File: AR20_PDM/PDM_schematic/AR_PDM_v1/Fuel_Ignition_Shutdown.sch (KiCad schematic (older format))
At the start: 16 parts

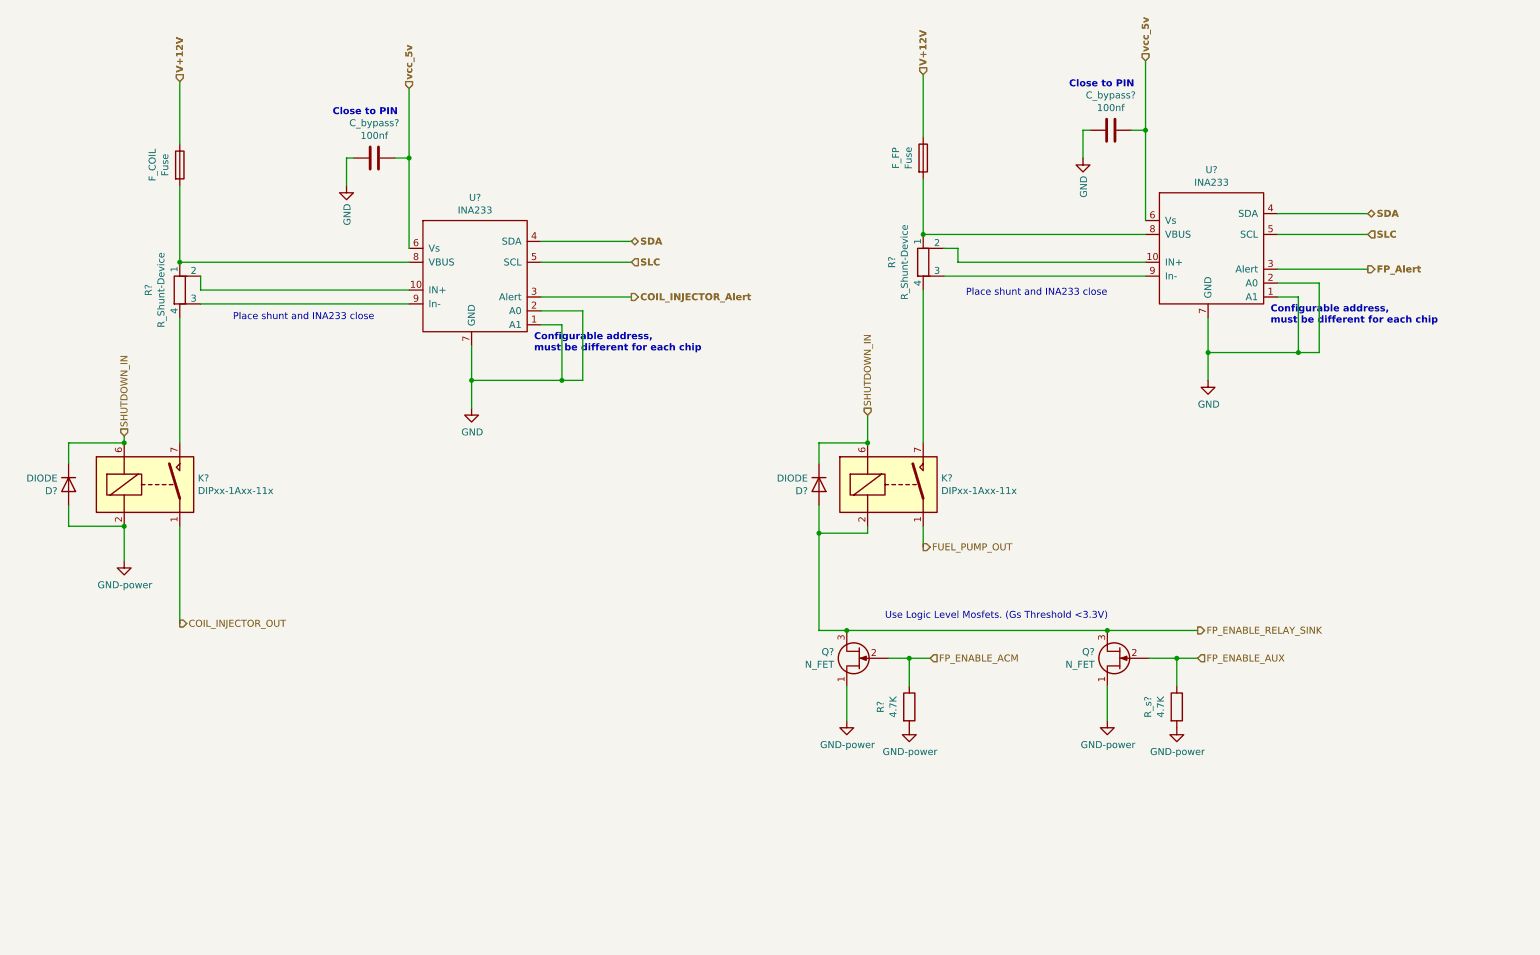
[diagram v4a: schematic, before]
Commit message: Fixed issues, controlled components, BOM, see discription
- added acm symbol
- fixed wrongly faced P-mosfets
- I/O expander now sinks led instead of source
- Bill of material mostly done
- Correct address for INA233 chips.
- Now 4 diodes serves as flyback for all mosfets
- Corrected naming scheme for compmonents (everything is not fixed yet)
- Fixed some labels
- altso some minor changes
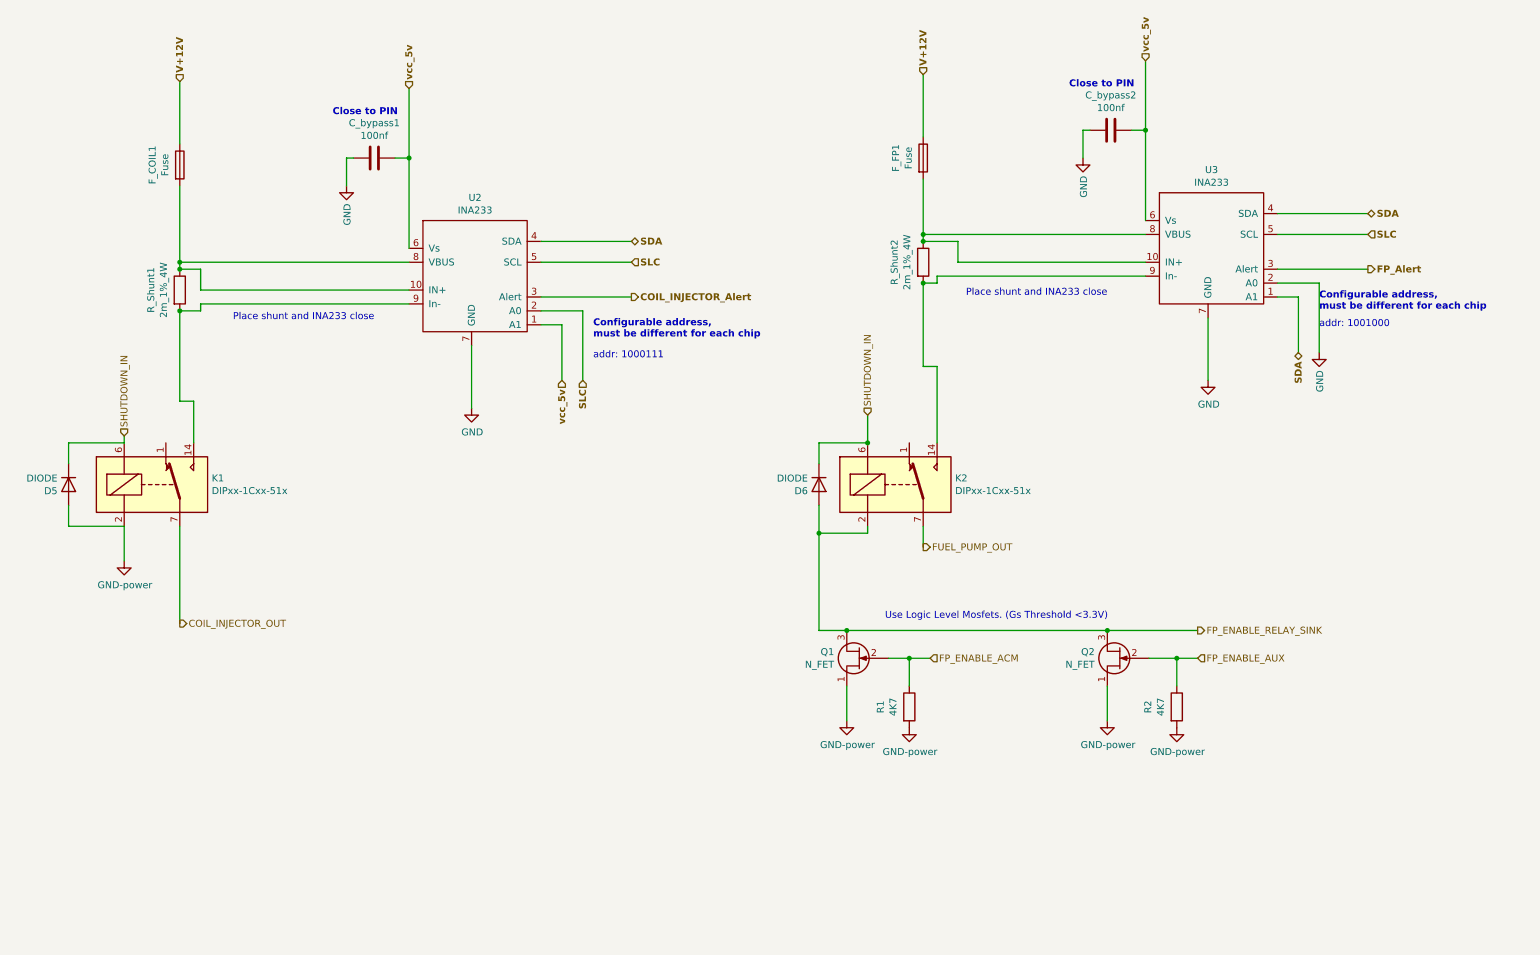
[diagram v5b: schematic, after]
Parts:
- removed K? (x2): DIPxx-1Axx-11x, Relay_THT:Relay_StandexMeder_DIP_LowProfile, symbol Relay:DIPxx-1Axx-11x
- removed R? (x2): R_Shunt-Device, symbol AR20_PDM_v1-rescue:R_Shunt-Device
- added K1, K2: DIPxx-1Cxx-51x, Relay_THT:Relay_StandexMeder_DIP_LowProfile, symbol Relay:DIPxx-1Cxx-51x
- added R_Shunt1, R_Shunt2: 2m_1%_4W, symbol AR20_PDM_v1-rescue:R-Device
- C_bypass1, C_bypass2: renamed from C_bypass?; footprint (none) -> Capacitor_SMD:C_0603_1608Metric
- R1, R2: renamed from R?; value 4.7K -> 4K7
- gave numbers to parts that had none: 6
- renumbered F_COIL to F_COIL1, F_FP to F_FP1
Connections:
- net COIL_INJECTOR_OUT: now also K1.7, K1.8
- net FP_ENABLE_RELAY_SINK: now also K2.2
- net FUEL_PUMP_OUT: now also K2.7, K2.8
- net GND: now also K1.2; no longer U2.1 (A1), U2.2 (A0), U3.1 (A1)
- net SDA: now also U3.1 (A1)
- net SHUTDOWN_IN: now also K1.6, K2.6
- net SLC: now also U2.2 (A0)
- net vcc_5v: now also U2.1 (A1)
- net at F_COIL1.2, U2.8 (VBUS): now also U2.10 (IN+), R_Shunt1.1
- net at U2.9 (In-): now also K1.14, R_Shunt1.2
- net at F_FP1.2, U3.8 (VBUS): now also U3.10 (IN+), R_Shunt2.1
- net at U3.9 (In-): now also K2.14, R_Shunt2.2
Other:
- note added: "addr: 1000111"
- note added: "addr: 1001000"

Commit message: PCB design, and issue fixing, work in progress
- Error fixed: Mux mosfet resistor change to ground
- Open drain output added on phase 6, for engine blipping purpose
- Most of pcb symbols and footprints are finished, including main connector
- PCB is change from 1oz to 2oz copper layer, for easier routing.
- Basic Draft of pcb is done, for now.
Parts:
- D5, D6: footprint (none) -> AR_PDM_v1:SODFL2512X73N; symbol AR20_PDM_v1-rescue:DIODE-Simulation_SPICE -> AR20_PDM_v1-rescue:DIODE-CustomSymbol
- F_COIL1, F_FP1: footprint (none) -> AR_PDM_v1:FuseHolder
- K1, K2: footprint Relay_THT:Relay_StandexMeder_DIP_LowProfile -> AR_PDM_v1:Relay; symbol Relay:DIPxx-1Cxx-51x -> AR20_PDM_v1-rescue:Relay
- Q8: renamed from Q1; footprint (none) -> Package_TO_SOT_SMD:SOT-23
- Q9: renamed from Q2; footprint (none) -> Package_TO_SOT_SMD:SOT-23
- R1, R2: footprint (none) -> Resistor_SMD:R_0603_1608Metric
- R_Shunt1, R_Shunt2: footprint (none) -> Resistor_SMD:R_2512_6332Metric
- U2, U3: footprint (none) -> AR_PDM_v1:INA233
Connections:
- net COIL_INJECTOR_OUT: no longer K1.8
- net FP_ENABLE_RELAY_SINK: now also D6.2 (A); no longer D6.1 (A)
- net FUEL_PUMP_OUT: no longer K2.8
- net GND: now also D5.2 (A); no longer D5.1 (A)
- net SHUTDOWN_IN: now also D5.1 (K), D6.1 (K); no longer D5.2 (K), D6.2 (K)
- no-connect marks 0 -> 2
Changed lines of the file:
@@
 	7350 4250 7350 4400
 $Comp
-L Device:Q_NJFET_DGS Q1
+L Device:Q_NJFET_DGS Q8
 U 1 1 5DDCBB71
 P 6900 5200
-F 0 "Q1" H 7091 5154 50  0000 L CNN
+F 0 "Q8" H 7091 5154 50  0000 L CNN
 F 1 "N_FET" H 7091 5245 50  0000 L CNN
-F 2 "" H 7100 5300 50  0001 C CNN
+F 2 "Package_TO_SOT_SMD:SOT-23" H 7100 5300 50  0001 C CNN
 F 3 "~" H 6900 5200 50  0001 C CNN
 	1    6900 5200
@@
 SHUTDOWN_IN
 $Comp
-L AR20_PDM_v1-rescue:DIODE-Simulation_SPICE D6
+L AR20_PDM_v1-rescue:DIODE-CustomSymbol D6
 U 1 1 5DDDEC0F
 P 6600 3950
 F 0 "D6" V 6554 4030 50  0000 L CNN
 F 1 "DIODE" V 6645 4030 50  0000 L CNN
-F 2 "" H 6600 3950 50  0001 C CNN
+F 2 "AR_PDM_v1:SODFL2512X73N" H 6600 3950 50  0001 C CNN
 F 3 "" H 6600 3950 50  0001 C CNN
 F 4 "Y" H 6600 3950 50  0001 L CNN "Spice_Netlist_Enabled"
@@
 	6800 5400 6800 5650
 $Comp
-L Device:Q_NJFET_DGS Q2
+L Device:Q_NJFET_DGS Q9
 U 1 1 5DDB5A55
 P 8775 5200
-F 0 "Q2" H 8966 5154 50  0000 L CNN
+F 0 "Q9" H 8966 5154 50  0000 L CNN
 F 1 "N_FET" H 8966 5245 50  0000 L CNN
-F 2 "" H 8975 5300 50  0001 C CNN
+F 2 "Package_TO_SOT_SMD:SOT-23" H 8975 5300 50  0001 C CNN
 F 3 "~" H 8775 5200 50  0001 C CNN
 	1    8775 5200
@@
 F 0 "R2" V 8968 5550 50  0000 C CNN
 F 1 "4K7" V 9059 5550 50  0000 C CNN
-F 2 "" V 9105 5550 50  0001 C CNN
+F 2 "Resistor_SMD:R_0603_1608Metric" V 9105 5550 50  0001 C CNN
 F 3 "~" H 9175 5550 50  0001 C CNN
 	1    9175 5550
@@
 F 0 "R1" V 7043 5550 50  0000 C CNN
 F 1 "4K7" V 7134 5550 50  0000 C CNN
-F 2 "" V 7180 5550 50  0001 C CNN
+F 2 "Resistor_SMD:R_0603_1608Metric" V 7180 5550 50  0001 C CNN
 F 3 "~" H 7250 5550 50  0001 C CNN
 	1    7250 5550
@@
 F 0 "F_FP1" V 7153 1600 50  0000 C CNN
 F 1 "Fuse" V 7244 1600 50  0000 C CNN
-F 2 "" V 7280 1600 50  0001 C CNN
+F 2 "AR_PDM_v1:FuseHolder" V 7280 1600 50  0001 C CNN
 F 3 "~" H 7350 1600 50  0001 C CNN
 	1    7350 1600
@@
 F 0 "U3" H 9425 2515 50  0000 C CNN
 F 1 "INA233" H 9425 2424 50  0000 C CNN
-F 2 "" H 9400 2100 50  0001 C CNN
+F 2 "AR_PDM_v1:INA233" H 9400 2100 50  0001 C CNN
 F 3 "" H 9400 2100 50  0001 C CNN
 	1    9400 2100
@@
 F 0 "U2" H 4125 2715 50  0000 C CNN
 F 1 "INA233" H 4125 2624 50  0000 C CNN
-F 2 "" H 4100 2300 50  0001 C CNN
+F 2 "AR_PDM_v1:INA233" H 4100 2300 50  0001 C CNN
 F 3 "" H 4100 2300 50  0001 C CNN
 	1    4100 2300
@@
 	1200 3650 1200 3800
 $Comp
-L AR20_PDM_v1-rescue:DIODE-Simulation_SPICE D5
+L AR20_PDM_v1-rescue:DIODE-CustomSymbol D5
 U 1 1 5DDCE100
 P 1200 3950
 F 0 "D5" V 1154 4030 50  0000 L CNN
 F 1 "DIODE" V 1245 4030 50  0000 L CNN
-F 2 "" H 1200 3950 50  0001 C CNN
+F 2 "AR_PDM_v1:SODFL2512X73N" H 1200 3950 50  0001 C CNN
 F 3 "" H 1200 3950 50  0001 C CNN
 F 4 "Y" H 1200 3950 50  0001 L CNN "Spice_Netlist_Enabled"
@@
 F 0 "F_COIL1" V 1803 1650 50  0000 C CNN
 F 1 "Fuse" V 1894 1650 50  0000 C CNN
-F 2 "" V 1930 1650 50  0001 C CNN
+F 2 "AR_PDM_v1:FuseHolder" V 1930 1650 50  0001 C CNN
 F 3 "~" H 2000 1650 50  0001 C CNN
 	1    2000 1650
@@
 F 0 "R_Shunt1" V 1793 2550 50  0000 C CNN
 F 1 "2m_1%_4W" V 1884 2550 50  0000 C CNN
-F 2 "" V 1930 2550 50  0001 C CNN
+F 2 "Resistor_SMD:R_2512_6332Metric" V 1930 2550 50  0001 C CNN
 F 3 "~" H 2000 2550 50  0001 C CNN
 	1    2000 2550
@@
 F 0 "R_Shunt2" V 7143 2350 50  0000 C CNN
 F 1 "2m_1%_4W" V 7234 2350 50  0000 C CNN
-F 2 "" V 7280 2350 50  0001 C CNN
+F 2 "Resistor_SMD:R_2512_6332Metric" V 7280 2350 50  0001 C CNN
 F 3 "~" H 7350 2350 50  0001 C CNN
 	1    7350 2350
@@
 	7350 2200 7600 2200
 $Comp
-L Relay:DIPxx-1Cxx-51x K2
+L AR20_PDM_v1-rescue:Relay K?
 U 1 1 5E1CE6DB
 P 7150 3950
+AR Path="/5E1CE6DB" Ref="K?"  Part="1"
+AR Path="/5DA8920B/5E1CE6DB" Ref="K2"  Part="1"
 F 0 "K2" H 7580 3996 50  0000 L CNN
 F 1 "DIPxx-1Cxx-51x" H 7580 3905 50  0000 L CNN
-F 2 "Relay_THT:Relay_StandexMeder_DIP_LowProfile" H 7600 3900 50  0001 L CNN
+F 2 "AR_PDM_v1:Relay" H 7600 3900 50  0001 L CNN
 F 3 "https://standexelectronics.com/wp-content/uploads/datasheet_reed_relay_DIP.pdf" H 7150 3950 50  0001 C CNN
 	1    7150 3950
@@
 Connection ~ 7350 2500
 $Comp
-L Relay:DIPxx-1Cxx-51x K1
+L AR20_PDM_v1-rescue:Relay K?
 U 1 1 5E1D8A96
 P 1800 3950
+AR Path="/5E1D8A96" Ref="K?"  Part="1"
+AR Path="/5DA8920B/5E1D8A96" Ref="K1"  Part="1"
 F 0 "K1" H 2230 3996 50  0000 L CNN
 F 1 "DIPxx-1Cxx-51x" H 2230 3905 50  0000 L CNN
-F 2 "Relay_THT:Relay_StandexMeder_DIP_LowProfile" H 2250 3900 50  0001 L CNN
+F 2 "AR_PDM_v1:Relay" H 2250 3900 50  0001 L CNN
 F 3 "https://standexelectronics.com/wp-content/uploads/datasheet_reed_relay_DIP.pdf" H 1800 3950 50  0001 C CNN
 	1    1800 3950
@@
 	1    0    0    -1
 $EndComp
+NoConn ~ 7250 3650
+NoConn ~ 1900 3650
 $EndSCHEMATC

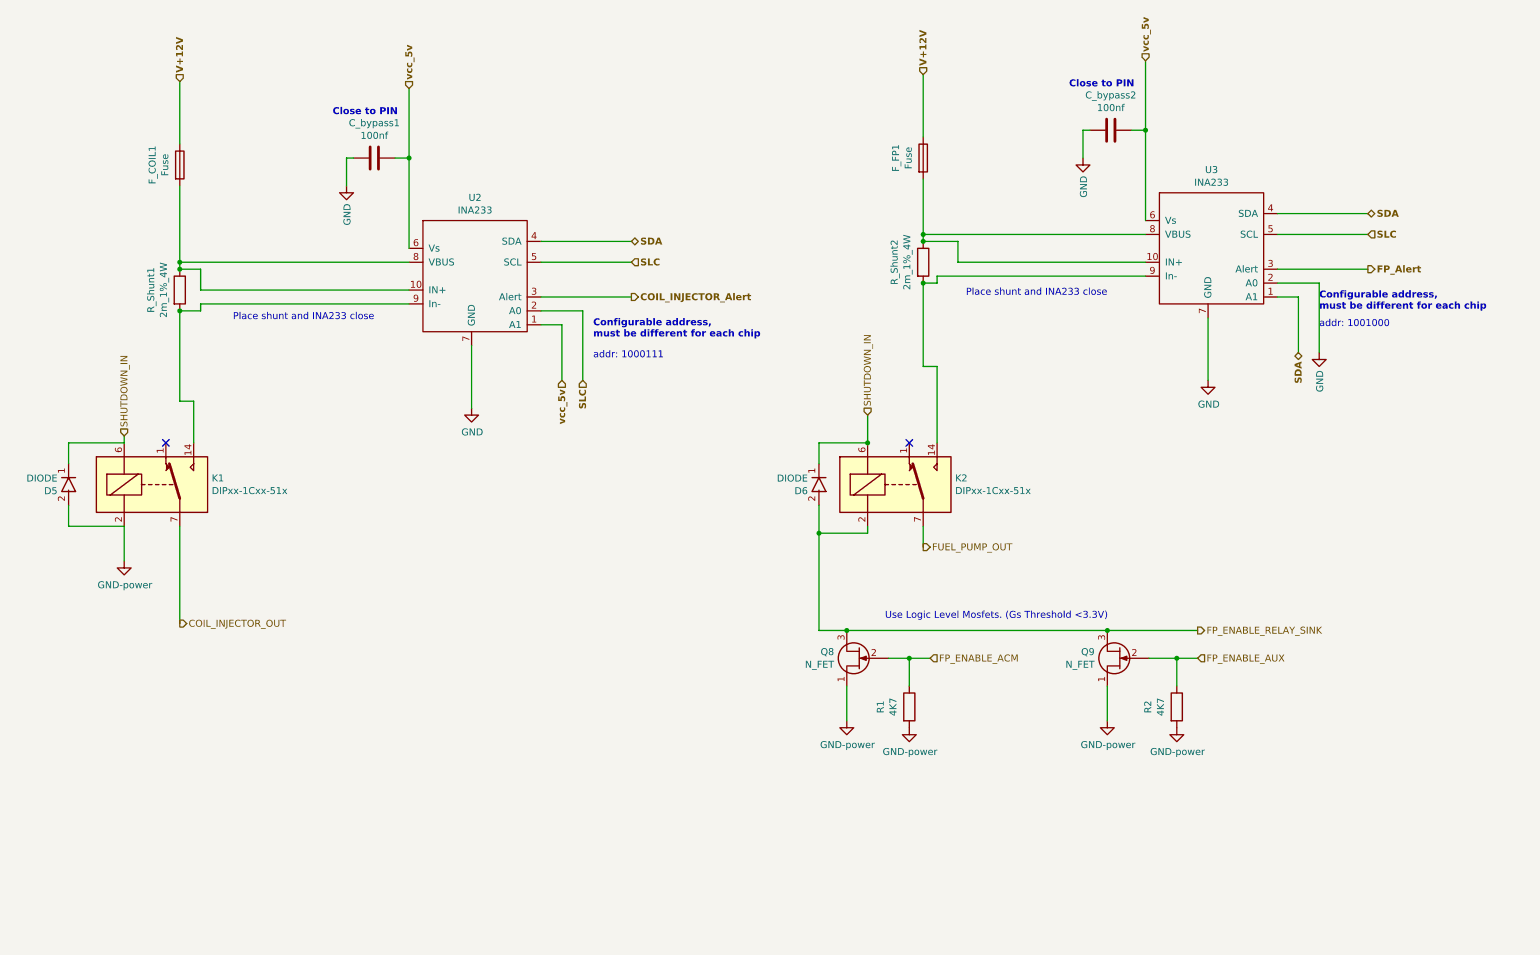
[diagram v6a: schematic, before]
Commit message: PCB design, and misc, see description, work in progress
- added shutdown circuit for ACM shutdown capability
PCB layout, in progress: 
- added copper pour for 12 volt, for fuses
- arranged indicator LED's
- arranged some of the P1-P7 caps and resistors
- re arranged P1-p7 in ascending order.
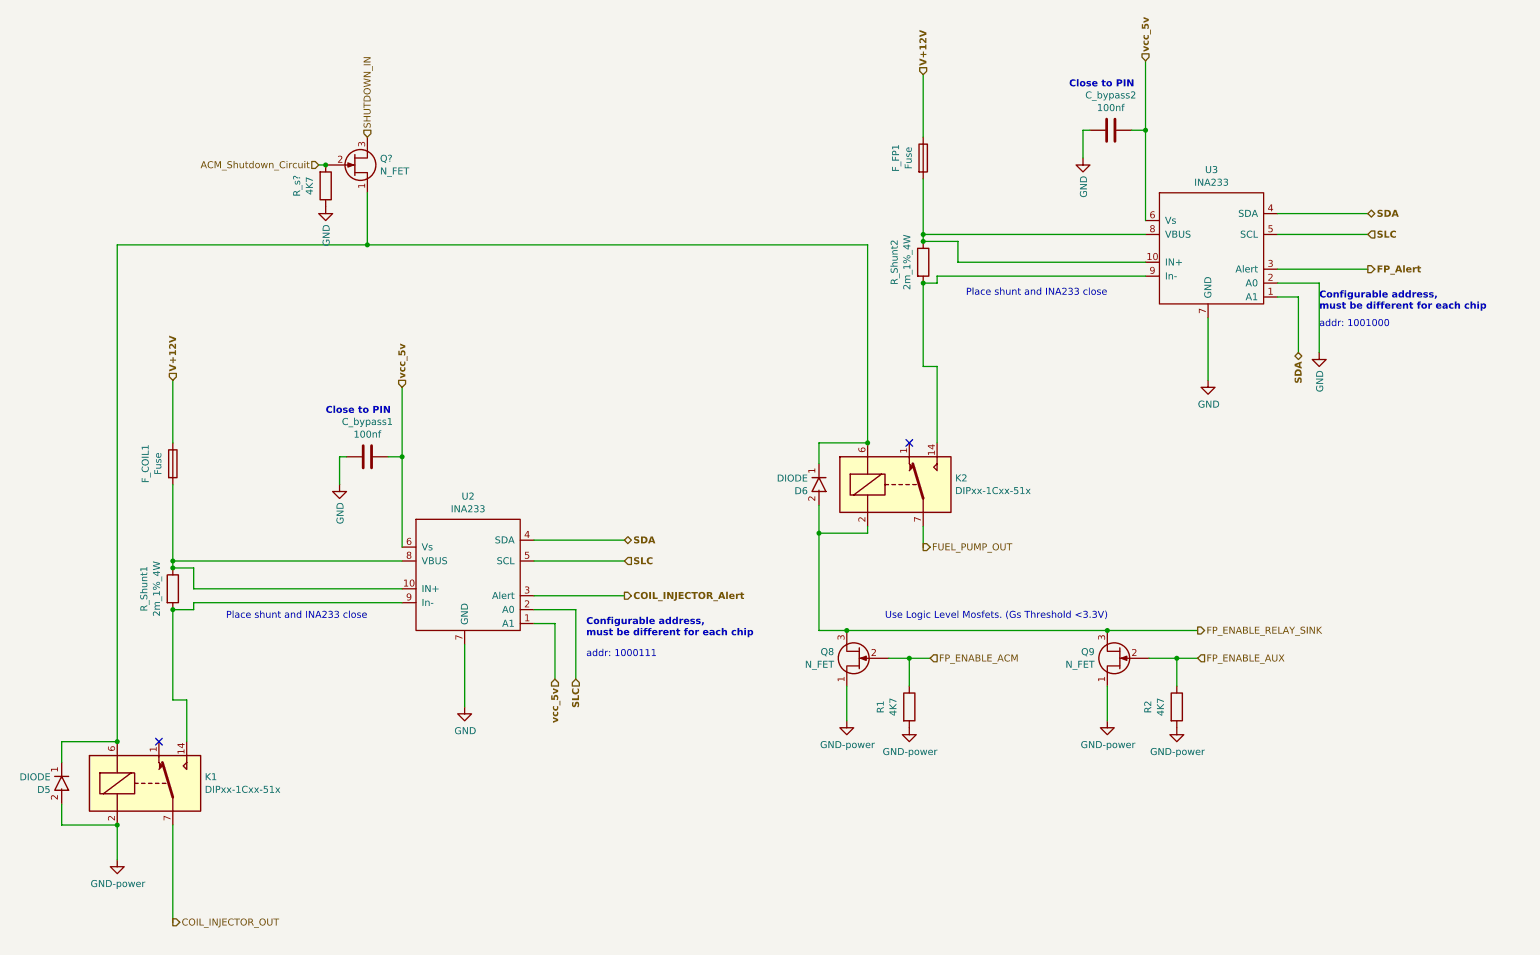
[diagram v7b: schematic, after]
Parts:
- added Q?: N_FET, Package_TO_SOT_SMD:SOT-23, symbol Device:Q_NJFET_DGS
- added R_s?: 4K7, Resistor_SMD:R_0603_1608Metric, symbol AR20_PDM_v1-rescue:R-Device
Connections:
- net GND: now also R_s?.1
- net SHUTDOWN_IN: now also Q?.3 (S); no longer D5.1 (K), D6.1 (K), K1.6, K2.6
- new net: D5.1 (K), D6.1 (K), K1.6, K2.6, Q?.1 (D)
- new net ACM_Shutdown_Circuit: Q?.2 (G), R_s?.2
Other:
- moved on the sheet: C_bypass1, D5, F_COIL1, K1, R_Shunt1, U2

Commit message: PCB Design, Work in progress
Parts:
- gave numbers to parts that had none: 2
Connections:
- net SHUTDOWN_Led: now reaches D5.1 (K), D6.1 (K), K1.6, K2.6, Q18.1 (D)
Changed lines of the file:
@@
 $Descr A4 11693 8268
 encoding utf-8
-Sheet 2 13
+Sheet 13 13
 Title ""
 Date ""
@@
 P 3050 1800
 AR Path="/5DA89415/5E265800" Ref="R_s?"  Part="1"
-AR Path="/5DA8920B/5E265800" Ref="R_s?"  Part="1"
+AR Path="/5DA8920B/5E265800" Ref="R_s13"  Part="1"
 AR Path="/5E2546F2/5E265800" Ref="R_s?"  Part="1"
 AR Path="/5E0FDCCC/5E265800" Ref="R_s?"  Part="1"
-F 0 "R_s?" V 2843 1800 50  0000 C CNN
+F 0 "R_s13" V 2843 1800 50  0000 C CNN
 F 1 "4K7" V 2934 1800 50  0000 C CNN
 F 2 "Resistor_SMD:R_0603_1608Metric" V 2980 1800 50  0001 C CNN
@@
 $EndComp
 $Comp
-L Device:Q_NJFET_DGS Q?
+L Device:Q_NJFET_DGS Q18
 U 1 1 5E265806
 P 3250 1650
-AR Path="/5DA8920B/5E265806" Ref="Q?"  Part="1"
+AR Path="/5DA8920B/5E265806" Ref="Q18"  Part="1"
 AR Path="/5E2546F2/5E265806" Ref="Q?"  Part="1"
 AR Path="/5E0FDCCC/5E265806" Ref="Q?"  Part="1"
-F 0 "Q?" H 3441 1604 50  0000 L CNN
+F 0 "Q18" H 3441 1604 50  0000 L CNN
 F 1 "N_FET" H 3441 1695 50  0000 L CNN
 F 2 "Package_TO_SOT_SMD:SOT-23" H 3450 1750 50  0001 C CNN
@@
 AR Path="/5E10174B/5E26DC54" Ref="#PWR?"  Part="1"
 AR Path="/5E1AEC18/5E26DC54" Ref="#PWR?"  Part="1"
-F 0 "#PWR?" H 3050 1700 50  0001 C CNN
+AR Path="/5DA8920B/5E26DC54" Ref="#PWR0132"  Part="1"
+F 0 "#PWR0132" H 3050 1700 50  0001 C CNN
 F 1 "GND" V 3055 1822 50  0000 R CNN
 F 2 "" H 3050 1950 50  0001 C CNN
@@
 	6950 2225 6950 3650
 Wire Wire Line
-	3350 2225 6950 2225
+	3350 2225 4300 2225
 Connection ~ 3350 2225
+Wire Wire Line
+	4300 2225 4300 1900
+Connection ~ 4300 2225
+Wire Wire Line
+	4300 2225 6950 2225
+Text HLabel 4300 1900 1    50   Output ~ 0
+SHUTDOWN_Led
 $EndSCHEMATC
